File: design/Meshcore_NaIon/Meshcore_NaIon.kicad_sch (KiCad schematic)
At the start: 28 parts, among them J7 SOLAR 12V, J8 Na-ion 1S, Q1 AO3401A, U1 CN3722

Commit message: Publish Mesh Repeater S4.16: routing fixes, COLD option and readable board labels
Update the editable KiCad project, seven-page schematic, portable footprints and 3D models, assembly variants, BOM, previews and independent CAD proofs. Preserve FakeTec GPIO compatibility. Manufacturing release remains paused.
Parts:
- added R56: 1.8 ohm 1% 0.125W, Meshcore:R_0805_2012Metric, symbol Meshcore:R_H
- added TP9: SOLAR, Meshcore:TestPoint_Pad_D1.5mm, symbol Meshcore:TP
- R3: value 6.34k 0.1% -> 61.9k 0.1% <=25ppm/C; MPN RQ73C2A6K34BTD -> RT0805BRD0761K9L; MPN_LTO_2S MPN not selected -> RT0805BRD07121KL; MPN_NaIon RQ73C2A6K34BTD -> RT0805BRD0761K9L; Nominal Na:6.34k LTO:13k -> Na:61.9k LTO:121k; Value display 1 (none) -> 61.9k 0.1%; Value_LTO_2S 13k 0.1% <=25ppm/C -> 121k 0.1% <=25ppm/C; Value_NaIon 6.34k 0.1% -> 61.9k 0.1% <=25ppm/C; Vendor (none) -> Yageo / distributor; Vendor URL (none) -> https://www.digikey.com/en/products/detail/yageo/RT0805BRD0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
- R4: value 10k 0.1% -> 100k 0.1% <=25ppm/C; MPN RT0805BRD0710KL -> RT0805BRD07100KL; MPN_LTO_2S MPN not selected -> RT0805BRD07100KL; MPN_NaIon RT0805BRD0710KL -> RT0805BRD07100KL; Nominal Na:10k LTO:10.5k -> Na:100k LTO:100k; Value display 1 (none) -> 100k 0.1%; Value_LTO_2S 10.5k 0.1% <=25ppm/C -> 100k 0.1% <=25ppm/C; Value_NaIon 10k 0.1% -> 100k 0.1% <=25ppm/C; Vendor (none) -> ChipDip / Yageo; Vendor URL (none) -> https://www.chipdip.ru/product/0.125vt-0805-100-kom-0.1-rt0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
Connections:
- net CS_P: now also R56.1; no longer R1.1
- net SOLAR: now also TP9.1
- new net CHG_CS_M: R1.1, R56.2
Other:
- added sheet 7. Thermal (Thermal.kicad_sch)
- note added: "7. Холод / опция"
- note added: "Kelvin: CSP до R56; BAT после R1"
- note added: "Na-ion / опция: R56 = 1,8 Ом; холод ≈ 96 мА; тепло ≈ 665 мА. Управление: лист 7. LTO / без опции: R56 = 0 Ом; узел листа 7 не ставить. R1 = 0,28 Ом: ток ≈ 714 мА, максимум ≈ 784 мА."
- note added: "Na-ion: R3 61,9k / R4 100k; C30 12pF; CV ≈ 3,915 В LTO 2S: R3 121k / R4 100k; C30 6,8pF; CV ≈ 5,345 В Делитель: 0,1%; ТКС ≤25 ppm/°C. LTO: запаять балансир."
- note added: "RC0805FR-071R8L"
- note added: "RT0805BRD07100KL"
- note added: "RT0805BRD0761K9L"
- note added: "S4.15 / 2026-10-11 / инженерный прототип"
- note added: "SOLAR"
- note removed: "Kelvin от R1"
- note removed: "Na-ion: R3 6,34k / R4 10k; C30 12pF; CV ≈ 3,948 В LTO 2S: R3 13k / R4 10,5k; C30 6,8pF; CV ≈ 5,408 В Делитель: 0,1%; LTO ТКС ≤25 ppm/°C. Запаять балансир."
- note removed: "R1 = 0,28 Ом / 1%: Iзар ≈ 714 мА; расчётный максимум ≈ 784 мА."
- note removed: "RQ73C2A6K34BTD"
- note removed: "RT0805BRD0710KL"
- note removed: "S4.12 / 2026-10-10 / инженерный прототип"
- moved on the sheet: C30, C4, D3, D4, J8, R1, R10, R11, R3, R4

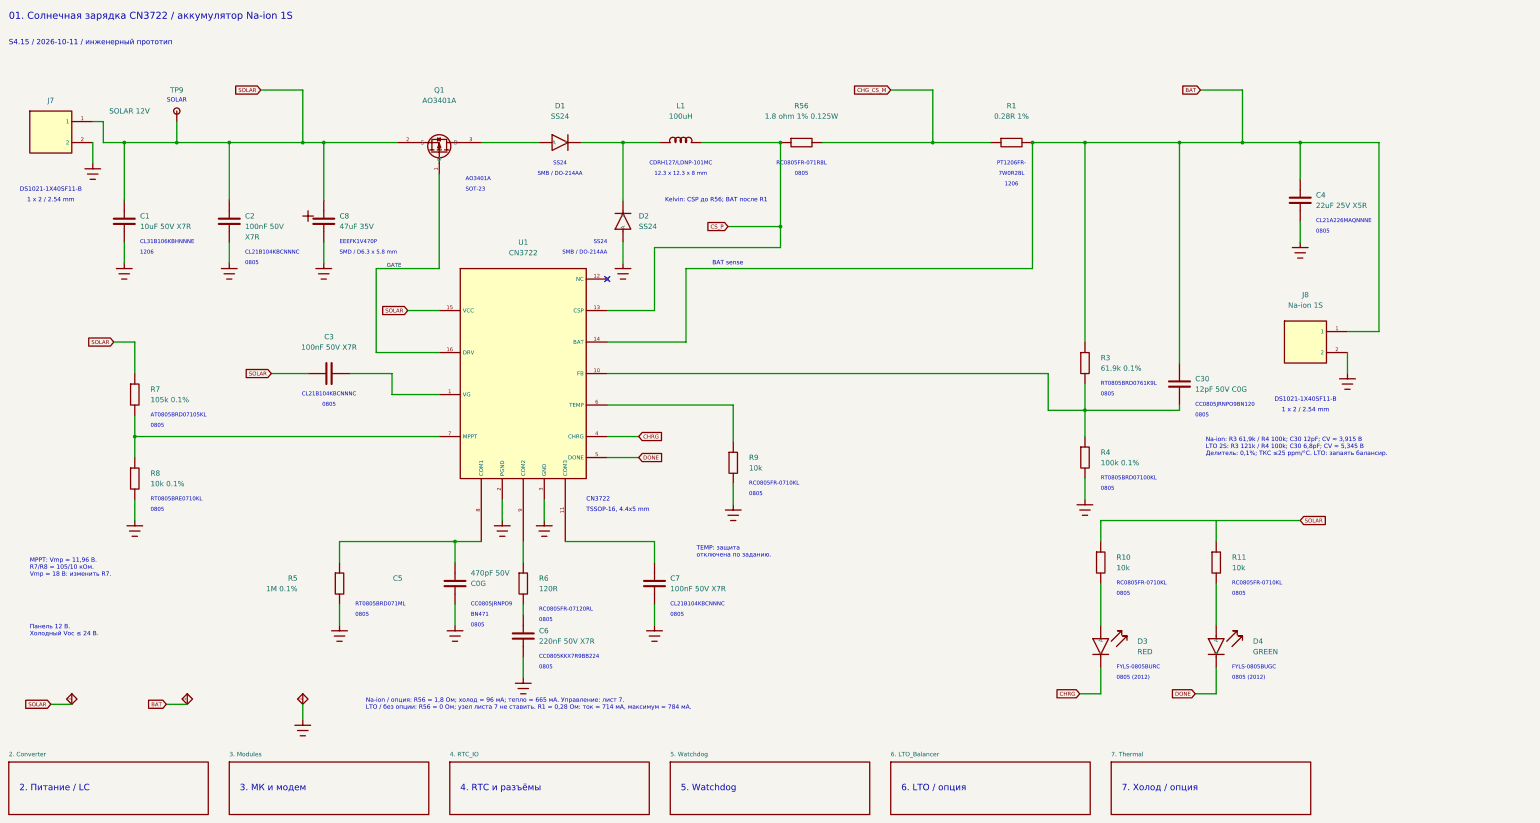
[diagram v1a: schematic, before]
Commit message: Publish S4.21 PCB and validated Rezonit manufacturing package
Update the public project to the accepted single-board S4.21 design, keeping
the user's manual routing improvements and removing SH1 and TP6.

Include the full editable KiCad project and local assets, three assembly BOM
variants, current assembly notes, eight-page schematic PDF, board views and
a clean nine-file Gerber/Excellon ZIP for Rezonit.

Validation: layout 29/29, power 14/14, CAM 59/59, publication integrity 18/18.
The committed native board and manufacturing ZIP match the verified byte
hashes. Preserve the existing licensing notices and watchdog source.
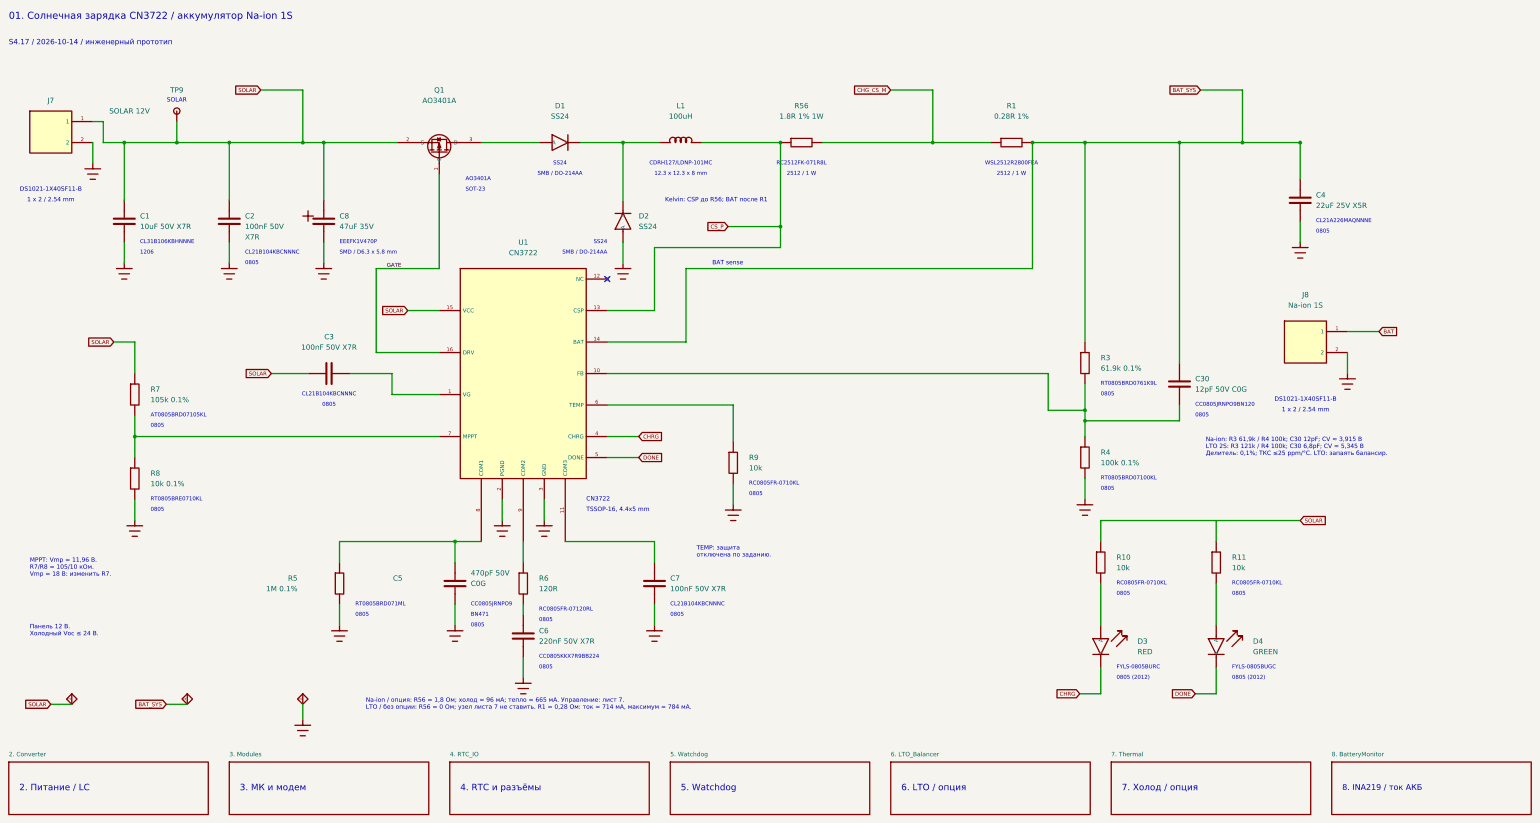
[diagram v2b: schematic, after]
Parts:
- C1: Fit_NaIon_NoCold (none) -> yes; MPN_NaIon_NoCold (none) -> CL31B106KBHNNNE; Value_NaIon_NoCold (none) -> 10uF 50V X7R
- C2, C3, C7: Fit_NaIon_NoCold (none) -> yes; MPN_NaIon_NoCold (none) -> CL21B104KBCNNNC; Value_NaIon_NoCold (none) -> 100nF 50V X7R
- C30: Fit_NaIon_NoCold (none) -> yes; MPN_NaIon_NoCold (none) -> CC0805JRNPO9BN120; Value_NaIon_NoCold (none) -> 12pF 50V C0G
- C4: Fit_NaIon_NoCold (none) -> yes; MPN_NaIon_NoCold (none) -> CL21A226MAQNNNE; Value_NaIon_NoCold (none) -> 22uF 25V X5R
- C5: Fit_NaIon_NoCold (none) -> yes; MPN_NaIon_NoCold (none) -> CC0805JRNPO9BN471; Value_NaIon_NoCold (none) -> 470pF 50V C0G
- C6: Fit_NaIon_NoCold (none) -> yes; MPN_NaIon_NoCold (none) -> CC0805KKX7R9BB224; Value_NaIon_NoCold (none) -> 220nF 50V X7R
- C8: Fit_NaIon_NoCold (none) -> yes; MPN_NaIon_NoCold (none) -> EEEFK1V470P; Value_NaIon_NoCold (none) -> 47uF 35V
- D1, D2: Fit_NaIon_NoCold (none) -> yes; MPN_NaIon_NoCold (none) -> SS24; Value_NaIon_NoCold (none) -> SS24
- D3: Fit_NaIon_NoCold (none) -> yes; MPN_NaIon_NoCold (none) -> FYLS-0805BURC; Value_NaIon_NoCold (none) -> RED
- D4: Fit_NaIon_NoCold (none) -> yes; MPN_NaIon_NoCold (none) -> FYLS-0805BUGC; Value_NaIon_NoCold (none) -> GREEN
- J7: Fit_NaIon_NoCold (none) -> yes; MPN_NaIon_NoCold (none) -> DS1021-1X40SF11-B; Value_NaIon_NoCold (none) -> SOLAR 12V
- J8: Fit_NaIon_NoCold (none) -> yes; MPN_NaIon_NoCold (none) -> DS1021-1X40SF11-B; Value_NaIon_NoCold (none) -> Na-ion 1S
- L1: Fit_NaIon_NoCold (none) -> yes; MPN_NaIon_NoCold (none) -> CDRH127/LDNP-101MC; Value_NaIon_NoCold (none) -> 100uH
- Q1: Fit_NaIon_NoCold (none) -> yes; MPN_NaIon_NoCold (none) -> AO3401A; Value_NaIon_NoCold (none) -> AO3401A
- R1: footprint Meshcore:R_1206_3216Metric -> Meshcore:R_Vishay_WSL2512_A3__A3_R1; Fit_NaIon_NoCold (none) -> yes; LCSC C5710536 -> (none); MPN PT1206FR-7W0R28L -> WSL2512R2800FEA; MPN_LTO_2S PT1206FR-7W0R28L -> WSL2512R2800FEA; MPN_NaIon PT1206FR-7W0R28L -> WSL2512R2800FEA; MPN_NaIon_NoCold (none) -> WSL2512R2800FEA; Package (none) -> 2512 / 1 W; Value_NaIon_NoCold (none) -> 0.28R 1%
- R10, R11, R9: Fit_NaIon_NoCold (none) -> yes; MPN_NaIon_NoCold (none) -> RC0805FR-0710KL; Value_NaIon_NoCold (none) -> 10k
- R3: Fit_NaIon_NoCold (none) -> yes; MPN_NaIon_NoCold (none) -> RT0805BRD0761K9L; Value_NaIon_NoCold (none) -> 61.9k 0.1% <=25ppm/C
- R4: Fit_NaIon_NoCold (none) -> yes; MPN_NaIon_NoCold (none) -> RT0805BRD07100KL; Value_NaIon_NoCold (none) -> 100k 0.1% <=25ppm/C
- R5: Fit_NaIon_NoCold (none) -> yes; MPN_NaIon_NoCold (none) -> RT0805BRD071ML; Value_NaIon_NoCold (none) -> 1M 0.1%
- R56: value 1.8 ohm 1% 0.125W -> 1.8R 1% 1W; footprint Meshcore:R_0805_2012Metric -> Meshcore:R_2512_6332Metric__A3_R56; Fit_NaIon_NoCold (none) -> yes; MPN RC0805FR-071R8L -> RC2512FK-071R8L; MPN_LTO_2S RC0805JR-070RL -> RC2512JK-070RL; MPN_NaIon RC0805FR-071R8L -> RC2512FK-071R8L; MPN_NaIon_NoCold (none) -> RC2512JK-070RL; Package (none) -> 2512 / 1 W; Value_NaIon 1.8 ohm 1% 0.125W -> 1.8R 1% 1W; Value_NaIon_NoCold (none) -> 0R jumper; Vendor URL https://www.danomsk.ru/shop/6-rezistory/86-rezistory-postoy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 -> (none)
- R6: Fit_NaIon_NoCold (none) -> yes; MPN_NaIon_NoCold (none) -> RC0805FR-07120RL; Value_NaIon_NoCold (none) -> 120R
- R7: Fit_NaIon_NoCold (none) -> yes; MPN_NaIon_NoCold (none) -> AT0805BRD07105KL; Value_NaIon_NoCold (none) -> 105k 0.1%
- R8: Fit_NaIon_NoCold (none) -> yes; MPN_NaIon_NoCold (none) -> RT0805BRE0710KL; Value_NaIon_NoCold (none) -> 10k 0.1%
- TP9: Fit_NaIon_NoCold (none) -> yes; MPN_NaIon_NoCold (none) -> PCB test pad / not purchased; Value_NaIon_NoCold (none) -> SOLAR
- U1: Fit_NaIon_NoCold (none) -> yes; MPN_NaIon_NoCold (none) -> CN3722; Value_NaIon_NoCold (none) -> CN3722
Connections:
- net BAT: no longer C30.1, C4.1, R1.2, R3.1, U1.14 (BAT)
- new net BAT_SYS: C30.1, C4.1, R1.2, R3.1, U1.14 (BAT)
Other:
- added sheet 8. BatteryMonitor (BatteryMonitor.kicad_sch)
- note added: "2512 / 1 W"
- note added: "8. INA219 / ток АКБ"
- note added: "RC2512FK-071R8L"
- note added: "S4.17 / 2026-10-14 / инженерный прототип"
- note added: "WSL2512R2800FEA"
- note removed: "7W0R28L"
- note removed: "PT1206FR-"
- note removed: "RC0805FR-071R8L"
- note removed: "S4.15 / 2026-10-11 / инженерный прототип"
